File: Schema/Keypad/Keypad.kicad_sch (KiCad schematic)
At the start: 72 parts, among them J1 JSTBATT, J2 Conn_01x04_Socket, J3 Conn_01x03_Socket, Q1 2N7002, Q2 AO3401A, Q4 2N7002, SW1 SW_SPDT, U1 BQ24075RGT, U2 nRF52840_holyiot_18010, U3 XC6206PxxxMR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

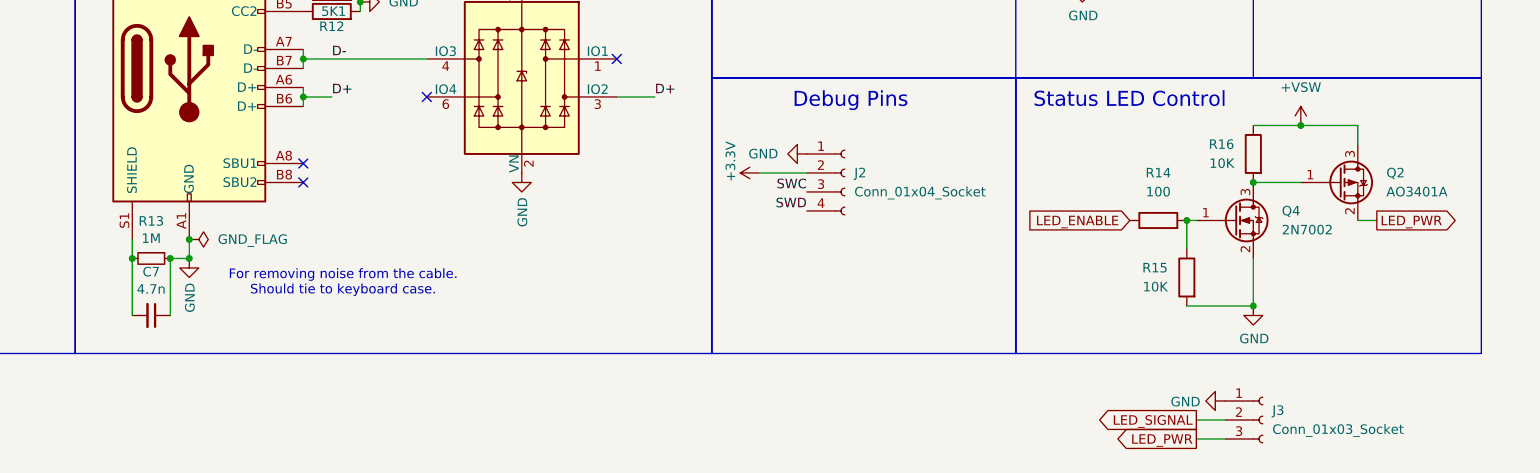
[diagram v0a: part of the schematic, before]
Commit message: Updating with enclosure
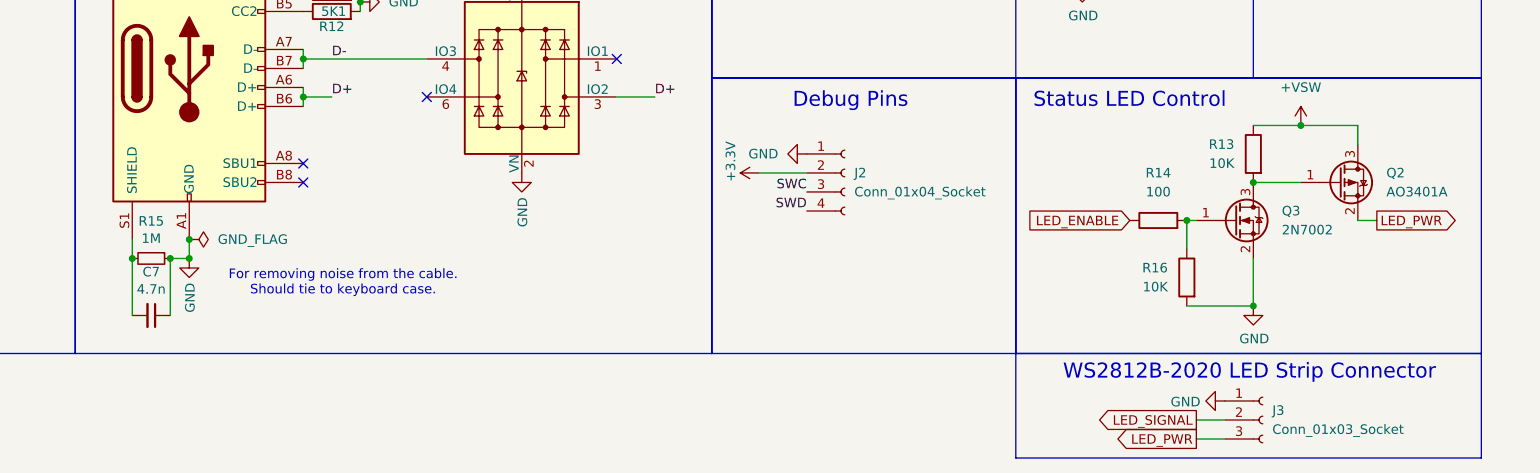
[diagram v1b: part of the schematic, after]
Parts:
- renumbered Q4 to Q3, R16 to R13, R13 to R15, R15 to R16
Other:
- note added: "WS2812B-2020 LED Strip Connector"
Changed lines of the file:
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@@
 	)
 	(rectangle
+		(start 236.22 201.93)
+		(end 298.45 215.9)
+		(stroke
+			(width 0)
+			(type default)
+		)
+		(fill
+			(type none)
+		)
+	)
+	(rectangle
 		(start 236.22 165.1)
 		(end 298.45 201.93)
@@
 		)
 	)
+	(text "WS2812B-2020 LED Strip Connector\n"
+		(exclude_from_sim no)
+		(at 267.462 204.47 0)
+		(effects
+			(font
+				(size 2 2)
+			)
+		)
+	)
 	(text "USB"
 		(exclude_from_sim no)
@@
 		(dnp no)
 		(fields_autoplaced yes)
-		(property "Reference" "#PWR028"
+		(property "Reference" "#PWR029"
 			(at 201.93 175.26 0)
 			(effects
@@
 			(project "Keypad"
 				(path "/2a4ce1bc-102b-4df8-a91e-406dbf25ad11"
-					(reference "#PWR028")
+					(reference "#PWR029")
 					(unit 1)
 				)
@@
 		(on_board yes)
 		(dnp no)
-		(property "Reference" "R16"
+		(property "Reference" "R13"
 			(at 265.43 173.9899 0)
 			(effects
@@
 			(project "Keypad"
 				(path "/2a4ce1bc-102b-4df8-a91e-406dbf25ad11"
-					(reference "R16")
+					(reference "R13")
 					(unit 1)
 				)
@@
 		(dnp no)
 		(fields_autoplaced yes)
-		(property "Reference" "#PWR033"
+		(property "Reference" "#PWR028"
 			(at 274.32 175.26 0)
 			(effects
@@
 			(project "Keypad"
 				(path "/2a4ce1bc-102b-4df8-a91e-406dbf25ad11"
-					(reference "#PWR033")
+					(reference "#PWR028")
 					(unit 1)
 				)
@@
 		(on_board yes)
 		(dnp no)
-		(property "Reference" "R15"
+		(property "Reference" "R16"
 			(at 256.54 190.4999 0)
 			(effects
@@
 			(project "Keypad"
 				(path "/2a4ce1bc-102b-4df8-a91e-406dbf25ad11"
-					(reference "R15")
+					(reference "R16")
 					(unit 1)
 				)
@@
 		(on_board yes)
 		(dnp no)
-		(property "Reference" "#PWR031"
+		(property "Reference" "#PWR032"
 			(at 125.73 195.58 0)
 			(effects
@@
 			(project "Keypad"
 				(path "/2a4ce1bc-102b-4df8-a91e-406dbf25ad11"
-					(reference "#PWR031")
+					(reference "#PWR032")
 					(unit 1)
 				)
@@
 		(on_board yes)
 		(dnp no)
-		(property "Reference" "#PWR032"
+		(property "Reference" "#PWR033"
 			(at 267.97 201.93 0)
 			(effects
@@
 			(project "Keypad"
 				(path "/2a4ce1bc-102b-4df8-a91e-406dbf25ad11"
-					(reference "#PWR032")
+					(reference "#PWR033")
 					(unit 1)
 				)
@@
 		(on_board yes)
 		(dnp no)
-		(property "Reference" "R13"
+		(property "Reference" "R15"
 			(at 120.65 184.2516 90)
 			(effects
@@
 			(project "Keypad"
 				(path "/2a4ce1bc-102b-4df8-a91e-406dbf25ad11"
-					(reference "R13")
+					(reference "R15")
 					(unit 1)
 				)
@@
 		(on_board yes)
 		(dnp no)
-		(property "Reference" "#PWR030"
+		(property "Reference" "#PWR031"
 			(at 205.74 177.8 0)
 			(effects
@@
 			(project "Keypad"
 				(path "/2a4ce1bc-102b-4df8-a91e-406dbf25ad11"
-					(reference "#PWR030")
+					(reference "#PWR031")
 					(unit 1)
 				)
@@
 		(dnp no)
 		(fields_autoplaced yes)
-		(property "Reference" "Q4"
+		(property "Reference" "Q3"
 			(at 271.78 182.8799 0)
 			(effects
@@
 			(project "Keypad"
 				(path "/2a4ce1bc-102b-4df8-a91e-406dbf25ad11"
-					(reference "Q4")
+					(reference "Q3")
 					(unit 1)
 				)
@@
 		(on_board yes)
 		(dnp no)
-		(property "Reference" "#PWR029"
+		(property "Reference" "#PWR030"
 			(at 170.18 184.15 0)
 			(effects
@@
 			(project "Keypad"
 				(path "/2a4ce1bc-102b-4df8-a91e-406dbf25ad11"
-					(reference "#PWR029")
+					(reference "#PWR030")
 					(unit 1)
 				)
